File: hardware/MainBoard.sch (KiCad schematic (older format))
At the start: 50 parts, among them J10 B2_HDR_LEFT, J11 B2_HDR_RIGHT, J12 ISP, J9 POWER, Q1 2N3904, Q2 2N3904, Q3 2N3904, U1 ATtiny85, U2 TL074, U3 78L05, U4 79L05

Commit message: [JNTUB-HW] Some PCB and schematic updates
* Thicker silkscreen on diodes
* Give explicit values to some items
* Update potentiometer schematic symbols
* Fix some symbol names
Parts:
- D1, D3: footprint Diodes_THT:D_DO-35_SOD27_P2.54mm_Vertical_AnodeUp -> SDIY:D_DO-35_SOD27_P2.54mm_Vertical_AnodeUp
- D2, D4, D5: footprint Diodes_THT:D_DO-35_SOD27_P2.54mm_Vertical_KathodeUp -> SDIY:D_DO-35_SOD27_P2.54mm_Vertical_KathodeUp
- R10, R11, R12, R13, R14, R16, R18, R19, R2, R20, R22, R23, R24, R25, R26, R27, R28, R4, R5, R6, R8: footprint Resistors_THT:R_Axial_DIN0207_L6.3mm_D2.5mm_P2.54mm_Vertical -> SDIY:R_Axial_DIN0207_L6.3mm_D2.5mm_P2.54mm_Vertical
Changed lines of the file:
@@
 F 0 "R6" V 2830 1650 50  0000 C CNN
 F 1 "10k" V 2750 1650 50  0000 C CNN
-F 2 "Resistors_THT:R_Axial_DIN0207_L6.3mm_D2.5mm_P2.54mm_Vertical" V 2680 1650 50  0001 C CNN
+F 2 "SDIY:R_Axial_DIN0207_L6.3mm_D2.5mm_P2.54mm_Vertical" V 2680 1650 50  0001 C CNN
 F 3 "" H 2750 1650 50  0001 C CNN
 	1    2750 1650
@@
 F 0 "R5" V 2230 1650 50  0000 C CNN
 F 1 "10k" V 2150 1650 50  0000 C CNN
-F 2 "Resistors_THT:R_Axial_DIN0207_L6.3mm_D2.5mm_P2.54mm_Vertical" V 2080 1650 50  0001 C CNN
+F 2 "SDIY:R_Axial_DIN0207_L6.3mm_D2.5mm_P2.54mm_Vertical" V 2080 1650 50  0001 C CNN
 F 3 "" H 2150 1650 50  0001 C CNN
 	1    2150 1650
@@
 F 0 "R4" V 3780 1250 50  0000 C CNN
 F 1 "10k" V 3700 1250 50  0000 C CNN
-F 2 "Resistors_THT:R_Axial_DIN0207_L6.3mm_D2.5mm_P2.54mm_Vertical" V 3630 1250 50  0001 C CNN
+F 2 "SDIY:R_Axial_DIN0207_L6.3mm_D2.5mm_P2.54mm_Vertical" V 3630 1250 50  0001 C CNN
 F 3 "" H 3700 1250 50  0001 C CNN
 	1    3700 1250
@@
 F 0 "R2" V 3780 950 50  0000 C CNN
 F 1 "10k" V 3700 950 50  0000 C CNN
-F 2 "Resistors_THT:R_Axial_DIN0207_L6.3mm_D2.5mm_P2.54mm_Vertical" V 3630 950 50  0001 C CNN
+F 2 "SDIY:R_Axial_DIN0207_L6.3mm_D2.5mm_P2.54mm_Vertical" V 3630 950 50  0001 C CNN
 F 3 "" H 3700 950 50  0001 C CNN
 	1    3700 950
@@
 F 0 "D1" H 4450 1150 50  0000 C CNN
 F 1 "BAT81" H 4450 950 50  0001 C CNN
-F 2 "Diodes_THT:D_DO-35_SOD27_P2.54mm_Vertical_AnodeUp" H 4450 1050 50  0001 C CNN
+F 2 "SDIY:D_DO-35_SOD27_P2.54mm_Vertical_AnodeUp" H 4450 1050 50  0001 C CNN
 F 3 "" H 4450 1050 50  0001 C CNN
 	1    4450 1050
@@
 F 0 "D2" H 4450 1550 50  0000 C CNN
 F 1 "BAT81" H 4450 1350 50  0001 C CNN
-F 2 "Diodes_THT:D_DO-35_SOD27_P2.54mm_Vertical_KathodeUp" H 4450 1450 50  0001 C CNN
+F 2 "SDIY:D_DO-35_SOD27_P2.54mm_Vertical_KathodeUp" H 4450 1450 50  0001 C CNN
 F 3 "" H 4450 1450 50  0001 C CNN
 	1    4450 1450
@@
 F 0 "R12" V 2830 3350 50  0000 C CNN
 F 1 "10k" V 2750 3350 50  0000 C CNN
-F 2 "Resistors_THT:R_Axial_DIN0207_L6.3mm_D2.5mm_P2.54mm_Vertical" V 2680 3350 50  0001 C CNN
+F 2 "SDIY:R_Axial_DIN0207_L6.3mm_D2.5mm_P2.54mm_Vertical" V 2680 3350 50  0001 C CNN
 F 3 "" H 2750 3350 50  0001 C CNN
 	1    2750 3350
@@
 F 0 "R11" V 2230 3350 50  0000 C CNN
 F 1 "10k" V 2150 3350 50  0000 C CNN
-F 2 "Resistors_THT:R_Axial_DIN0207_L6.3mm_D2.5mm_P2.54mm_Vertical" V 2080 3350 50  0001 C CNN
+F 2 "SDIY:R_Axial_DIN0207_L6.3mm_D2.5mm_P2.54mm_Vertical" V 2080 3350 50  0001 C CNN
 F 3 "" H 2150 3350 50  0001 C CNN
 	1    2150 3350
@@
 F 0 "D3" H 4450 2800 50  0000 C CNN
 F 1 "BAT81" H 4450 2600 50  0001 C CNN
-F 2 "Diodes_THT:D_DO-35_SOD27_P2.54mm_Vertical_AnodeUp" H 4450 2700 50  0001 C CNN
+F 2 "SDIY:D_DO-35_SOD27_P2.54mm_Vertical_AnodeUp" H 4450 2700 50  0001 C CNN
 F 3 "" H 4450 2700 50  0001 C CNN
 	1    4450 2700
@@
 F 0 "D4" H 4450 3200 50  0000 C CNN
 F 1 "BAT81" H 4450 3000 50  0001 C CNN
-F 2 "Diodes_THT:D_DO-35_SOD27_P2.54mm_Vertical_KathodeUp" H 4450 3100 50  0001 C CNN
+F 2 "SDIY:D_DO-35_SOD27_P2.54mm_Vertical_KathodeUp" H 4450 3100 50  0001 C CNN
 F 3 "" H 4450 3100 50  0001 C CNN
 	1    4450 3100
@@
 F 0 "R16" V 2580 5025 50  0000 C CNN
 F 1 "1M" V 2500 5025 50  0000 C CNN
-F 2 "Resistors_THT:R_Axial_DIN0207_L6.3mm_D2.5mm_P2.54mm_Vertical" V 2430 5025 50  0001 C CNN
+F 2 "SDIY:R_Axial_DIN0207_L6.3mm_D2.5mm_P2.54mm_Vertical" V 2430 5025 50  0001 C CNN
 F 3 "" H 2500 5025 50  0001 C CNN
 	1    2500 5025
@@
 F 0 "R13" V 3430 4575 50  0000 C CNN
 F 1 "100k" V 3350 4575 50  0000 C CNN
-F 2 "Resistors_THT:R_Axial_DIN0207_L6.3mm_D2.5mm_P2.54mm_Vertical" V 3280 4575 50  0001 C CNN
+F 2 "SDIY:R_Axial_DIN0207_L6.3mm_D2.5mm_P2.54mm_Vertical" V 3280 4575 50  0001 C CNN
 F 3 "" H 3350 4575 50  0001 C CNN
 	1    3350 4575
@@
 F 0 "R19" V 5530 5175 50  0000 C CNN
 F 1 "R_led" V 5450 5175 40  0000 C CNN
-F 2 "Resistors_THT:R_Axial_DIN0207_L6.3mm_D2.5mm_P2.54mm_Vertical" V 5380 5175 50  0001 C CNN
+F 2 "SDIY:R_Axial_DIN0207_L6.3mm_D2.5mm_P2.54mm_Vertical" V 5380 5175 50  0001 C CNN
 F 3 "" H 5450 5175 50  0001 C CNN
 	1    5450 5175
@@
 F 0 "R25" V 3355 7250 50  0000 C CNN
 F 1 "100k .1%" V 3175 7250 50  0000 C CNN
-F 2 "Resistors_THT:R_Axial_DIN0207_L6.3mm_D2.5mm_P2.54mm_Vertical" V 3205 7250 50  0001 C CNN
+F 2 "SDIY:R_Axial_DIN0207_L6.3mm_D2.5mm_P2.54mm_Vertical" V 3205 7250 50  0001 C CNN
 F 3 "" H 3275 7250 50  0001 C CNN
 	1    3275 7250
@@
 F 0 "R24" V 2580 7250 50  0000 C CNN
 F 1 "100k .1%" V 2400 7250 50  0000 C CNN
-F 2 "Resistors_THT:R_Axial_DIN0207_L6.3mm_D2.5mm_P2.54mm_Vertical" V 2430 7250 50  0001 C CNN
+F 2 "SDIY:R_Axial_DIN0207_L6.3mm_D2.5mm_P2.54mm_Vertical" V 2430 7250 50  0001 C CNN
 F 3 "" H 2500 7250 50  0001 C CNN
 	1    2500 7250
@@
 F 0 "R22" V 2155 6600 50  0000 C CNN
 F 1 "100k" V 2075 6600 40  0000 C CNN
-F 2 "Resistors_THT:R_Axial_DIN0207_L6.3mm_D2.5mm_P2.54mm_Vertical" V 2005 6600 50  0001 C CNN
+F 2 "SDIY:R_Axial_DIN0207_L6.3mm_D2.5mm_P2.54mm_Vertical" V 2005 6600 50  0001 C CNN
 F 3 "" H 2075 6600 50  0001 C CNN
 	1    2075 6600
@@
 F 0 "R23" V 4605 6700 50  0000 C CNN
 F 1 "R_led" V 4525 6700 40  0000 C CNN
-F 2 "Resistors_THT:R_Axial_DIN0207_L6.3mm_D2.5mm_P2.54mm_Vertical" V 4455 6700 50  0001 C CNN
+F 2 "SDIY:R_Axial_DIN0207_L6.3mm_D2.5mm_P2.54mm_Vertical" V 4455 6700 50  0001 C CNN
 F 3 "" H 4525 6700 50  0001 C CNN
 	1    4525 6700
@@
 F 0 "D5" H 2950 5325 50  0000 C CNN
 F 1 "1N4148" H 2950 5125 50  0001 C CNN
-F 2 "Diodes_THT:D_DO-35_SOD27_P2.54mm_Vertical_KathodeUp" H 2950 5225 50  0001 C CNN
+F 2 "SDIY:D_DO-35_SOD27_P2.54mm_Vertical_KathodeUp" H 2950 5225 50  0001 C CNN
 F 3 "" H 2950 5225 50  0001 C CNN
 	1    2950 5225
@@
 F 0 "R10" V 3780 2900 50  0000 C CNN
 F 1 "10k" V 3700 2900 50  0000 C CNN
-F 2 "Resistors_THT:R_Axial_DIN0207_L6.3mm_D2.5mm_P2.54mm_Vertical" V 3630 2900 50  0001 C CNN
+F 2 "SDIY:R_Axial_DIN0207_L6.3mm_D2.5mm_P2.54mm_Vertical" V 3630 2900 50  0001 C CNN
 F 3 "" H 3700 2900 50  0001 C CNN
 	1    3700 2900
@@
 F 0 "R8" V 3780 2600 50  0000 C CNN
 F 1 "10k" V 3700 2600 50  0000 C CNN
-F 2 "Resistors_THT:R_Axial_DIN0207_L6.3mm_D2.5mm_P2.54mm_Vertical" V 3630 2600 50  0001 C CNN
+F 2 "SDIY:R_Axial_DIN0207_L6.3mm_D2.5mm_P2.54mm_Vertical" V 3630 2600 50  0001 C CNN
 F 3 "" H 3700 2600 50  0001 C CNN
 	1    3700 2600
@@
 F 0 "R20" V 5030 5575 50  0000 C CNN
 F 1 "100k" V 4950 5575 50  0000 C CNN
-F 2 "Resistors_THT:R_Axial_DIN0207_L6.3mm_D2.5mm_P2.54mm_Vertical" V 4880 5575 50  0001 C CNN
+F 2 "SDIY:R_Axial_DIN0207_L6.3mm_D2.5mm_P2.54mm_Vertical" V 4880 5575 50  0001 C CNN
 F 3 "" H 4950 5575 50  0001 C CNN
 	1    4950 5575
@@
 F 0 "R26" V 6855 2500 50  0000 C CNN
 F 1 "100k" V 6775 2500 50  0000 C CNN
-F 2 "Resistors_THT:R_Axial_DIN0207_L6.3mm_D2.5mm_P2.54mm_Vertical" V 6705 2500 50  0001 C CNN
+F 2 "SDIY:R_Axial_DIN0207_L6.3mm_D2.5mm_P2.54mm_Vertical" V 6705 2500 50  0001 C CNN
 F 3 "" H 6775 2500 50  0001 C CNN
 	1    6775 2500
@@
 F 0 "R27" V 2155 6100 50  0000 C CNN
 F 1 "10k" V 2075 6100 40  0000 C CNN
-F 2 "Resistors_THT:R_Axial_DIN0207_L6.3mm_D2.5mm_P2.54mm_Vertical" V 2005 6100 50  0001 C CNN
+F 2 "SDIY:R_Axial_DIN0207_L6.3mm_D2.5mm_P2.54mm_Vertical" V 2005 6100 50  0001 C CNN
 F 3 "" H 2075 6100 50  0001 C CNN
 	1    2075 6100
@@
 F 0 "R28" V 1755 6800 50  0000 C CNN
 F 1 "100k" V 1675 6800 50  0000 C CNN
-F 2 "Resistors_THT:R_Axial_DIN0207_L6.3mm_D2.5mm_P2.54mm_Vertical" V 1605 6800 50  0001 C CNN
+F 2 "SDIY:R_Axial_DIN0207_L6.3mm_D2.5mm_P2.54mm_Vertical" V 1605 6800 50  0001 C CNN
 F 3 "" H 1675 6800 50  0001 C CNN
 	1    1675 6800
@@
 F 0 "R14" V 4230 4575 50  0000 C CNN
 F 1 "47k" V 4150 4575 50  0000 C CNN
-F 2 "Resistors_THT:R_Axial_DIN0207_L6.3mm_D2.5mm_P2.54mm_Vertical" V 4080 4575 50  0001 C CNN
+F 2 "SDIY:R_Axial_DIN0207_L6.3mm_D2.5mm_P2.54mm_Vertical" V 4080 4575 50  0001 C CNN
 F 3 "" H 4150 4575 50  0001 C CNN
 	1    4150 4575
@@
 F 0 "R18" V 3830 5475 50  0000 C CNN
 F 1 "10k" V 3750 5475 50  0000 C CNN
-F 2 "Resistors_THT:R_Axial_DIN0207_L6.3mm_D2.5mm_P2.54mm_Vertical" V 3680 5475 50  0001 C CNN
+F 2 "SDIY:R_Axial_DIN0207_L6.3mm_D2.5mm_P2.54mm_Vertical" V 3680 5475 50  0001 C CNN
 F 3 "" H 3750 5475 50  0001 C CNN
 	1    3750 5475

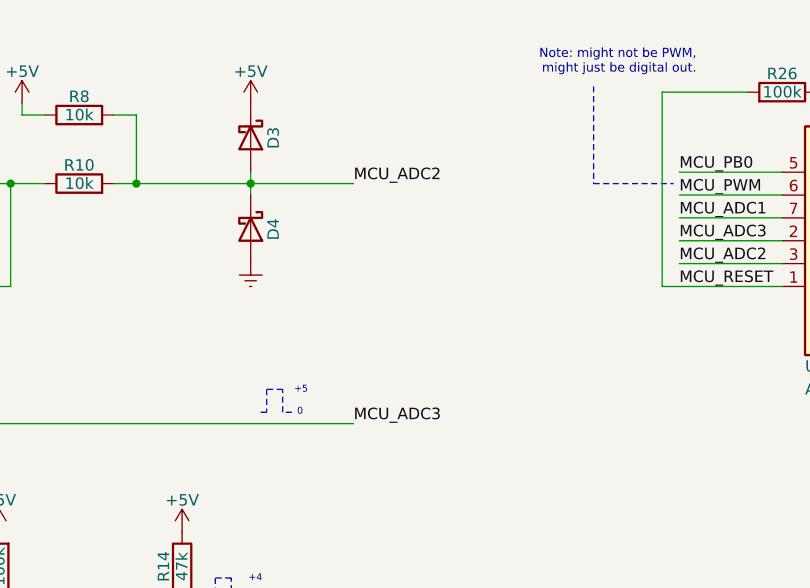
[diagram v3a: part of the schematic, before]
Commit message: [JNTUB-HW] Create SMD version of PCB
Use KiCad scripting API to write a script to turn most
through-hole parts into SMT parts. Will use this to release
two variants of the board.

Had to reroute many traces so that every through hole pad is
connected to traces on the front layer (that way, when all
the through holes are removed, the components are still
connected to traces).
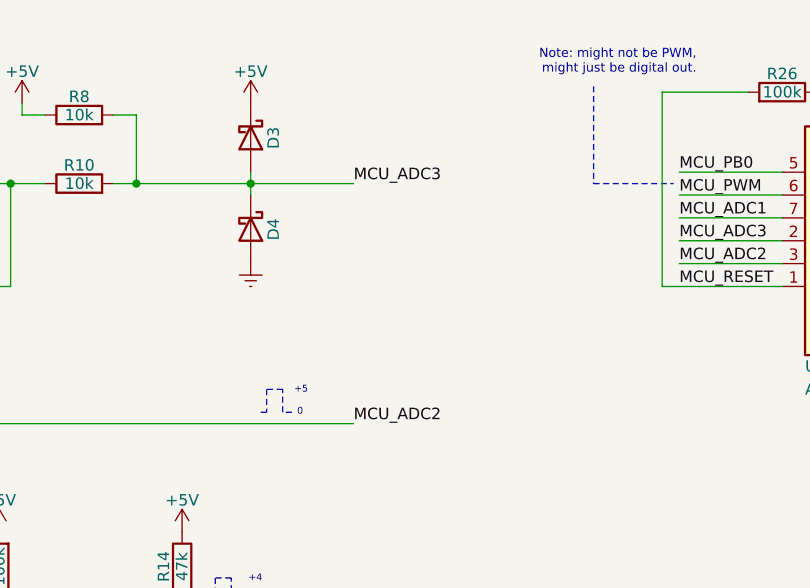
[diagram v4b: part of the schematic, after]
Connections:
- net MCU_ADC2: now also J10.6 (Pin_6); no longer D3.2 (A), D4.1 (K), R10.2, R8.2
- net MCU_ADC3: now also D3.2 (A), D4.1 (K), R10.2, R8.2; no longer J10.6 (Pin_6)
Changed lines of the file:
@@
 Text Label 6325 3250 0    50   ~ 0
 MCU_ADC2
-Text Label 4900 3950 0    50   ~ 0
+Text Label 4900 2900 0    50   ~ 0
 MCU_ADC3
 $Comp
@@
 Wire Wire Line
 	3850 1250 3950 1250
-Text Label 4900 2900 0    50   ~ 0
+Text Label 4900 3950 0    50   ~ 0
 MCU_ADC2
 $Comp

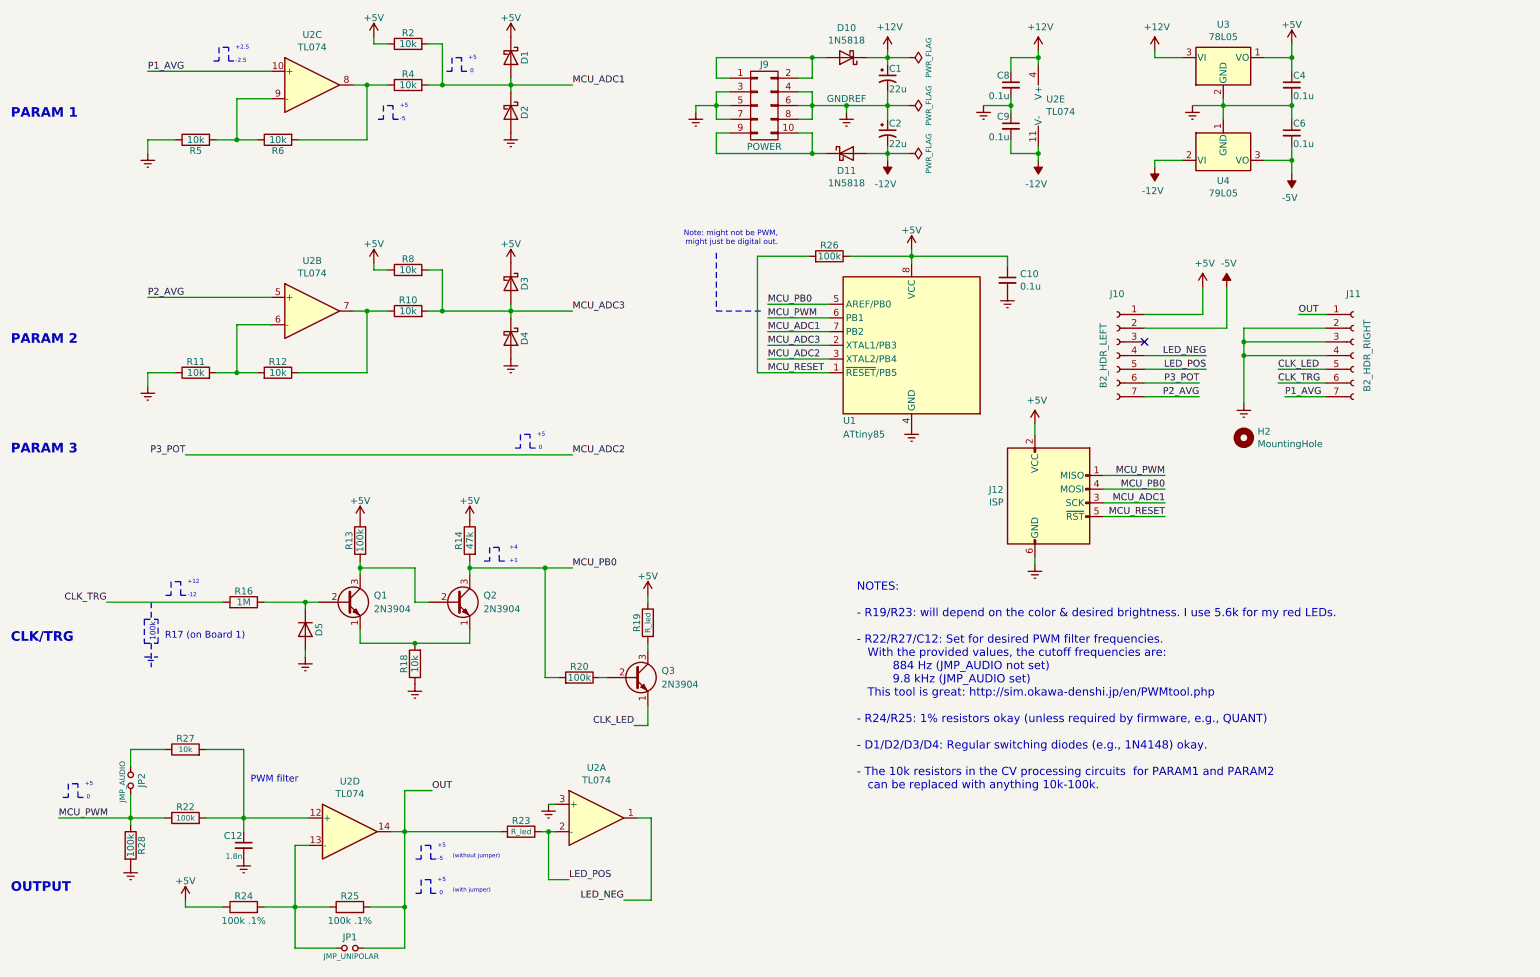
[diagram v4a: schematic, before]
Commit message: [JNTUB-HW] PCB now preparable for SMT assembly!
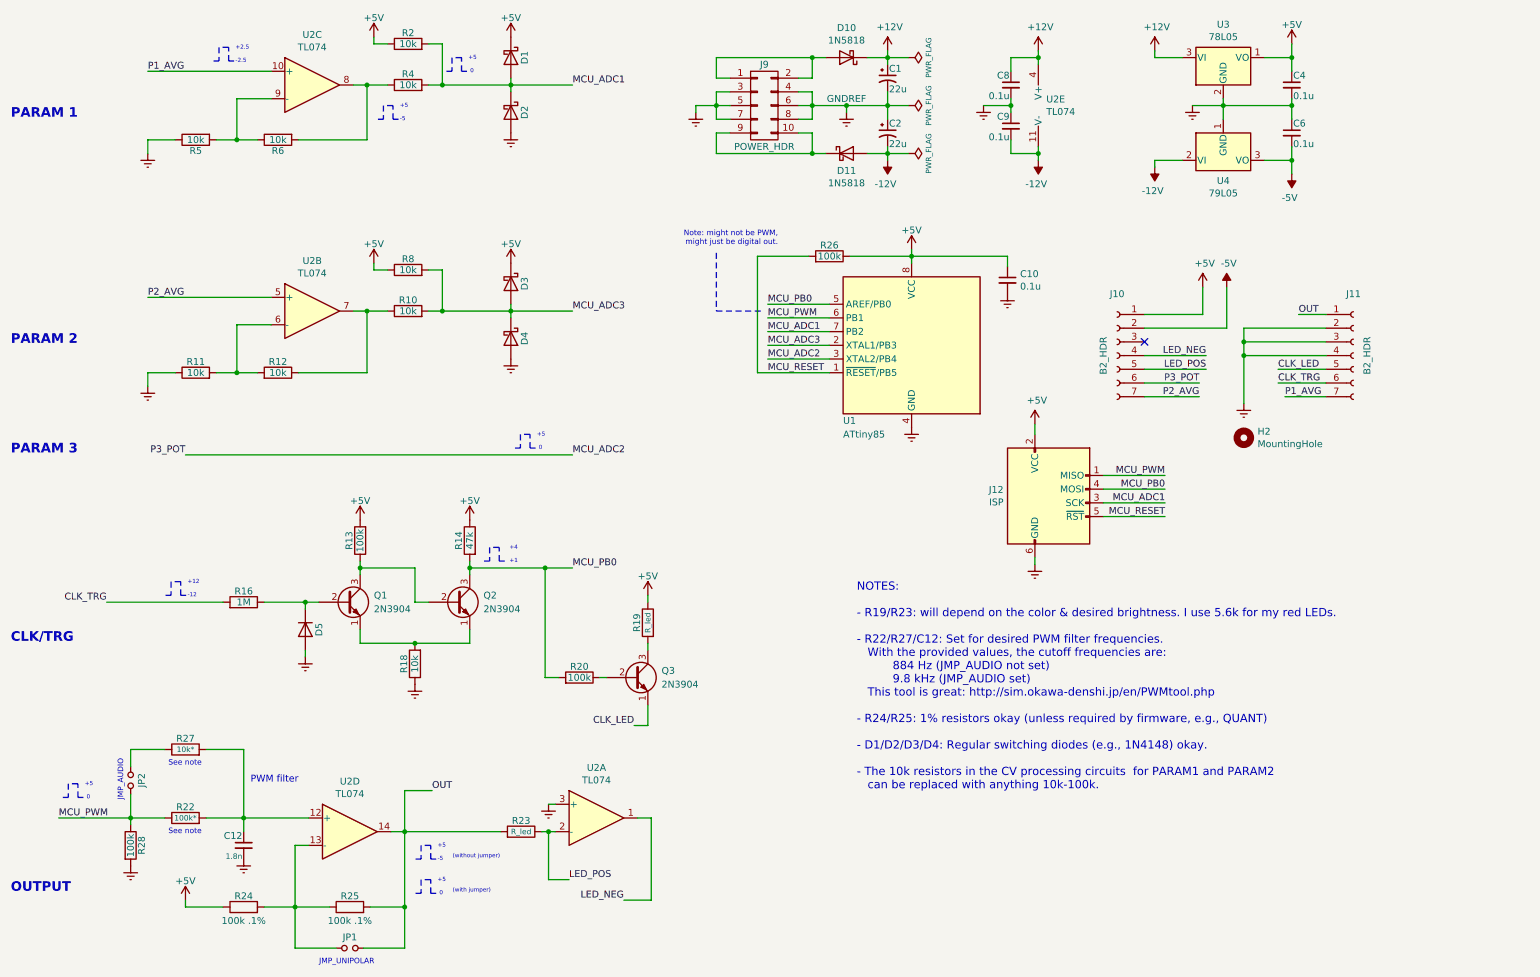
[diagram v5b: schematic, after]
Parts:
- C1, C2: LCSC (none) -> C336292; LCSCe (none) -> Yes; Note (none) -> At least 22uF; Power Rating (none) -> 35V; SMT Place (none) -> Yes; SMT package (none) -> CP_ELEC_5x5.3; Type (none) -> Electrolytic cap
- C10, C4, C6, C8, C9: LCSC (none) -> C49678; SMT Place (none) -> Yes; SMT package (none) -> C_0805; Type (none) -> Ceramic cap
- C12: LCSC (none) -> C28260; Note (none) -> See note about PWM filter; SMT Place (none) -> Yes; SMT Value (none) -> 2.2n; SMT package (none) -> C_0805; Type (none) -> Mylar / poly cap
- D1, D2, D3, D4: LCSC (none) -> C2128; Note (none) -> 1N4148 okay; SMT Note (none) -> BAT54: C21107 (extended); SMT Place (none) -> Yes; SMT package (none) -> SOD-323; Type (none) -> Schottky clamping diode
- D10, D11: LCSC (none) -> C8598; Note (none) -> Or 1N5819 or other equivalent; SMT Note (none) -> 5819; SMT Place (none) -> Yes; SMT package (none) -> SOD-123; Type (none) -> Schottky reverse protection diode
- D5: LCSC (none) -> C2128; SMT Place (none) -> Yes; SMT package (none) -> SOD-323; Type (none) -> Switching diode
- H2: Config (none) -> do not fit; Exclude (none) -> Yes
- J10: value B2_HDR_LEFT -> B2_HDR; Config (none) -> -smtmfg; Type (none) -> 1x7 Female Pin Header
- J11: value B2_HDR_RIGHT -> B2_HDR; Config (none) -> -smtmfg; Type (none) -> 1x7 Female Pin Header
- J12: Config (none) -> -smtmfg; Type (none) -> 2x3 Male Pin Header
- J9: value POWER -> POWER_HDR; Config (none) -> -smtmfg; Type (none) -> 2x5 Male Pin Header
- JP1: value JMP_UNIPOLAR -> JMP; Config (none) -> -smtmfg; Note (none) -> Plus 2x jumpers. Alternatively, you can solder in some wire.; Type (none) -> 1x2 Male Pin Header
- JP2: value JMP_AUDIO -> JMP; Config (none) -> -smtmfg; Note (none) -> Plus 2x jumpers. Alternatively, you can solder in some wire.; Type (none) -> 1x2 Male Pin Header
- Q1, Q2, Q3: LCSC (none) -> C20526; SMT Place (none) -> Yes; SMT package (none) -> SOT-23; Type (none) -> NPN Transistor
- R10, R11, R12, R18, R2, R4, R5, R6, R8: LCSC (none) -> C17414; SMT Place (none) -> Yes; SMT package (none) -> R_0805; Tolerance (none) -> 1%; Type (none) -> 1% Metal Film Resistor
- R13, R20, R26, R28: LCSC (none) -> C17407; SMT Place (none) -> Yes; SMT package (none) -> R_0805; Type (none) -> 5% Carbon Film Resistor
- R14: LCSC (none) -> C17713; SMT Place (none) -> Yes; SMT package (none) -> R_0805; Type (none) -> 5% Carbon Film Resistor
- R16: LCSC (none) -> C17514; SMT Place (none) -> Yes; SMT package (none) -> R_0805; Type (none) -> 5% Carbon Film Resistor
- R19, R23: Config (none) -> -smtmfg; Note (none) -> 5.6k, varies by LED; SMT package (none) -> Through-hole (can fit 0603); Type (none) -> 5% Carbon Film Resistor
- R22: value 100k -> 100k*; LCSC (none) -> C17801; Note (none) -> See note about PWM filter; SMT Place (none) -> Yes; SMT Value (none) -> 68k; SMT package (none) -> R_0805; Type (none) -> 1% Metal Film Resistor
- R24, R25: LCSC (none) -> C17407; Note (none) -> 1% okay if high precision not needed; SMT Note (none) -> 0.1%: C55868 (extended); SMT Place (none) -> Yes; SMT package (none) -> R_0805; Tolerance (none) -> 0.1%; Type (none) -> 0.1% Metal Film Resistor
- R27: value 10k -> 10k*; LCSC (none) -> C17828; Note (none) -> See note about PWM filter; SMT Place (none) -> Yes; SMT Value (none) -> 8.2k; SMT package (none) -> R_0805; Tolerance (none) -> 1%; Type (none) -> 1% Metal Film Resistor
- U1: Config (none) -> -smtmfg; SMT package (none) -> DIP 8 (NOT SOIC); Type (none) -> ATtiny85 Microcontroller
- U2: Config (none) -> -smtmfg; SMT package (none) -> DIP 14 (NOT SOIC); Type (none) -> TL074 Quad Op-Amp
- U3: LCSC (none) -> C71136; SMT Place (none) -> Yes; SMT package (none) -> SOT-89-3; Type (none) -> LM78L05 +5V Regulator
- U4: LCSC (none) -> C122849; LCSCe (none) -> Yes; SMT Place (none) -> Yes; SMT package (none) -> SOT-89-3; Type (none) -> LM79L05 -5V Regulator
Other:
- note added: "JMP_AUDIO"
- note added: "JMP_UNIPOLAR"
- note added: "See note"
- note removed: "100k"
- note removed: "R17 (on Board 1)"
